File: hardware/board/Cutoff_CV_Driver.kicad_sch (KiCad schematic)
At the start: 17 parts

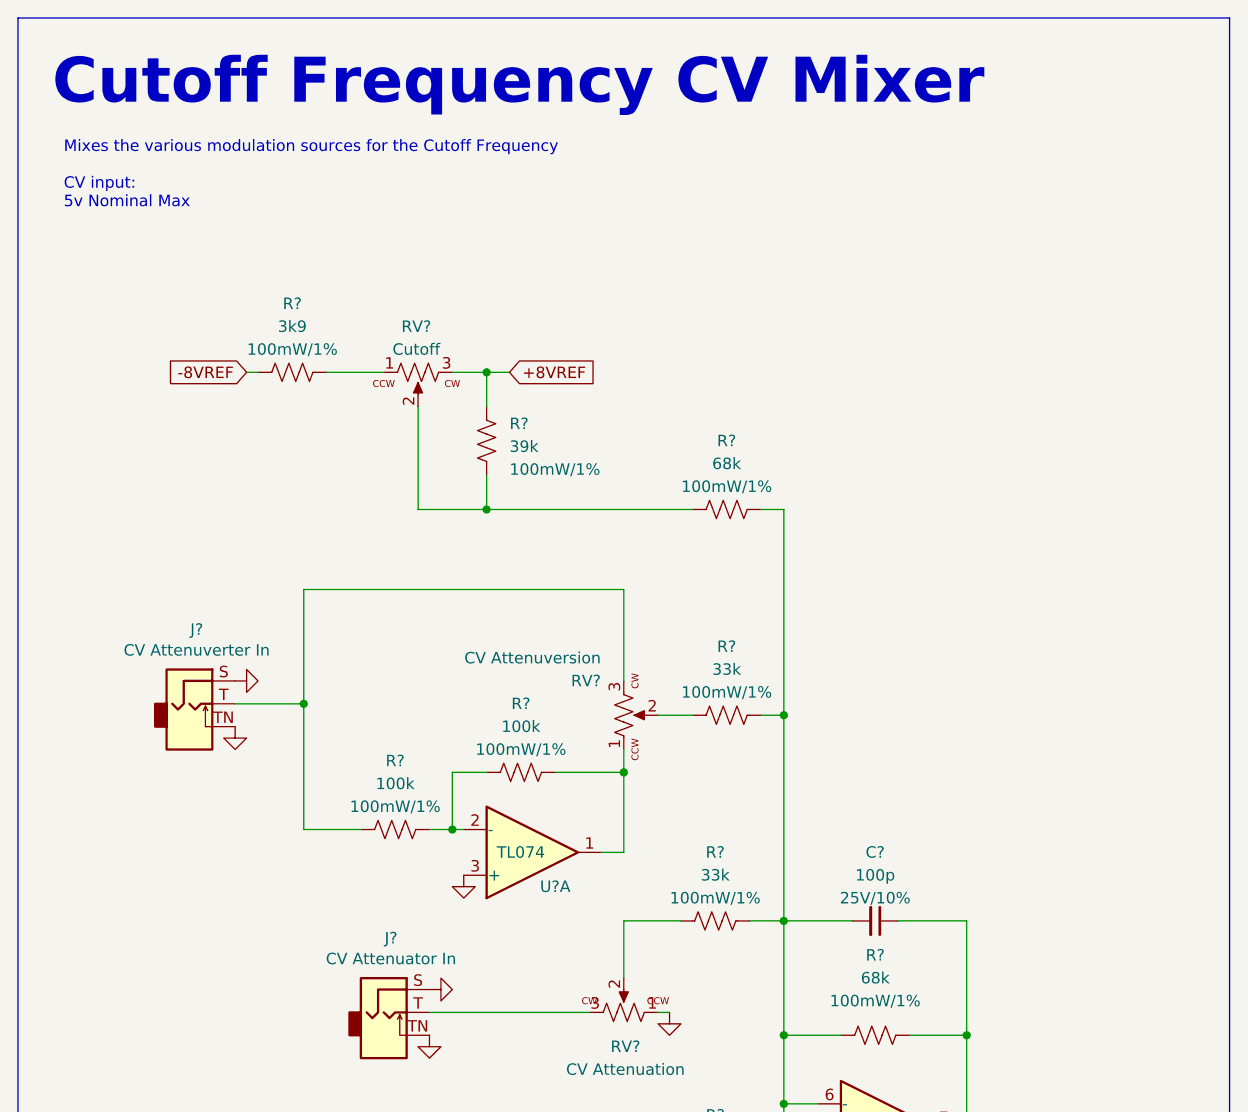
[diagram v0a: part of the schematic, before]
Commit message: Schematic getting closer to being finished
Schematic should be close to being ready to assign MPNs.
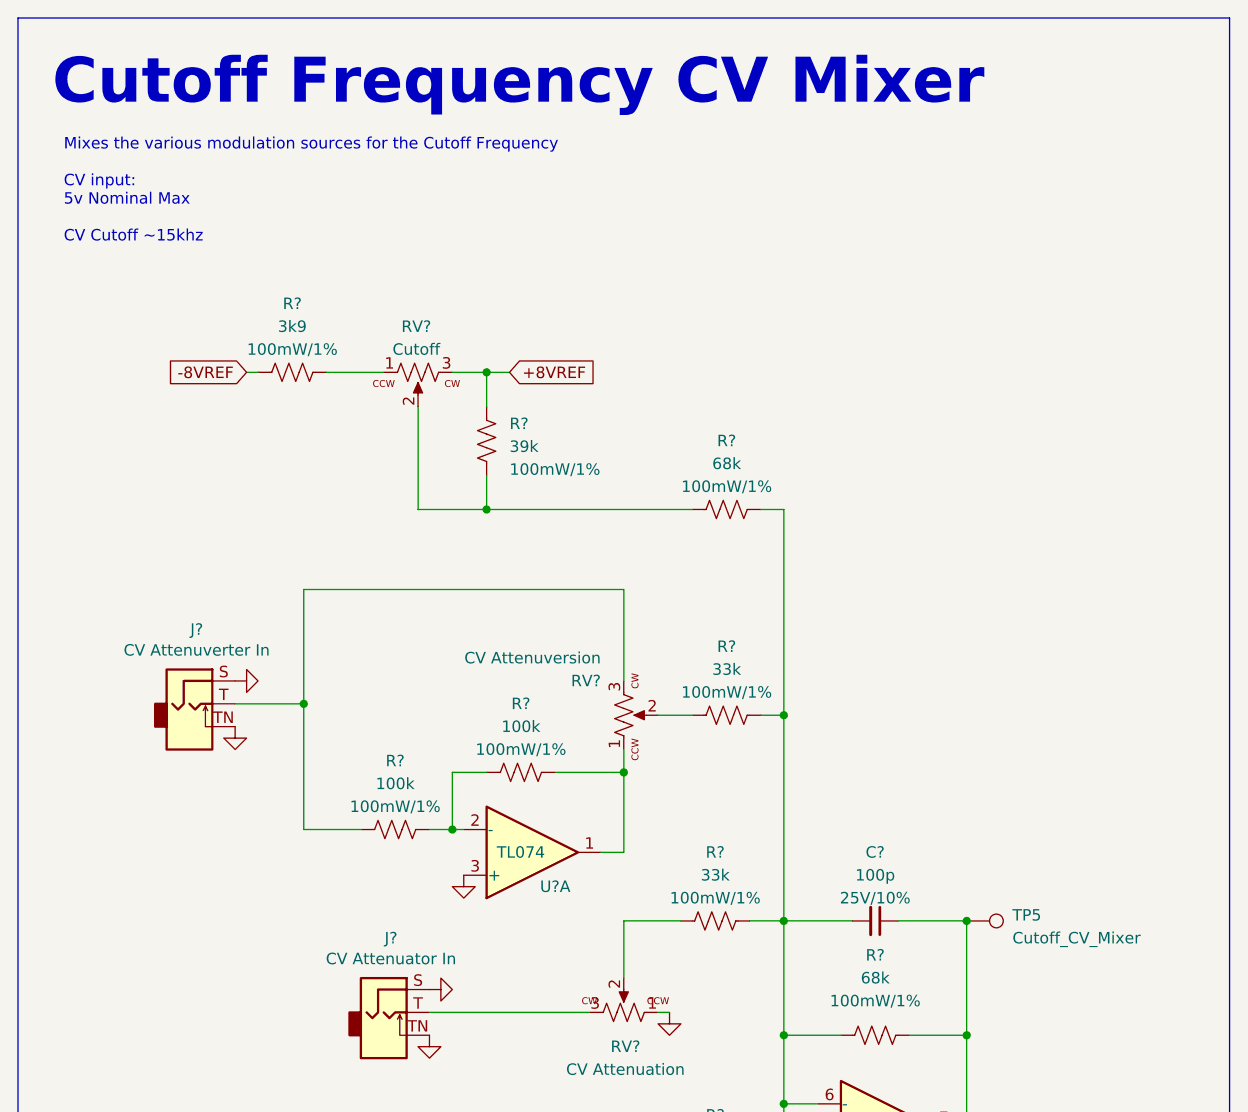
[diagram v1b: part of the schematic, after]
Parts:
- added TP5: Cutoff_CV_Mixer, symbol Connector:TestPoint
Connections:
- net CUTOFF_OUT: now also TP5.1
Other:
- note added: "Mixes the various modulation sources for the Cutoff Frequency CV input: 5v Nominal Max CV Cutoff ~15khz"
- note removed: "Mixes the various modulation sources for the Cutoff Frequency CV input: 5v Nominal Max"
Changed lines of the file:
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@@
   (junction (at 160.02 133.35) (diameter 0) (color 0 0 0 0)
   )
+  (junction (at 180.34 120.65) (diameter 0) (color 0 0 0 0)
+  )
   (junction (at 160.02 97.79) (diameter 0) (color 0 0 0 0)
   )
@@
     (stroke (width 0) (type default))
   )
+  (wire (pts (xy 180.34 120.65) (xy 180.34 133.35))
+    (stroke (width 0) (type default))
+  )
   (wire (pts (xy 127 59.69) (xy 127 63.5))
     (stroke (width 0) (type default))
@@
     (stroke (width 0) (type default))
   )
-  (wire (pts (xy 180.34 120.65) (xy 180.34 133.35))
-    (stroke (width 0) (type default))
-  )
   (wire (pts (xy 172.72 120.65) (xy 180.34 120.65))
     (stroke (width 0) (type default))
@@
     (fill (type none))
   )
-  (text "Mixes the various modulation sources for the Cutoff Frequency\n\nCV input:\n5v Nominal Max\n\n\n"
-    (at 80.01 45.72 0)
+  (text "Mixes the various modulation sources for the Cutoff Frequency\n\nCV input:\n5v Nominal Max\n\nCV Cutoff ~15khz\n\n\n"
+    (at 80.01 49.53 0)
     (effects (font (size 1.27 1.27)) (justify left bottom))
   )
@@
         )
       )
+    )
+  )
+  (symbol (lib_id "Connector:TestPoint") (at 180.34 120.65 270) (unit 1)
+    (in_bom yes) (on_board yes) (dnp no) (fields_autoplaced)
+    (property "Reference" "TP5" (at 185.42 120.015 90)
+      (effects (font (size 1.27 1.27)) (justify left))
+    )
+    (property "Value" "Cutoff_CV_Mixer" (at 185.42 122.555 90)
+      (effects (font (size 1.27 1.27)) (justify left))
+    )
+    (property "Footprint" "" (at 180.34 125.73 0)
+      (effects (font (size 1.27 1.27)) hide)
+    )
+    (property "Datasheet" "~" (at 180.34 125.73 0)
+      (effects (font (size 1.27 1.27)) hide)
+    )
+    (pin "1")
+    (instances
+      (project "mainboard"
+        (path "/960bd036-bf0c-45ea-9f41-1321756e0e5a/48d891c0-35ba-4c8e-a930-c990a10298eb"
+          (reference "TP5") (unit 1)
+        )
+        (path "/960bd036-bf0c-45ea-9f41-1321756e0e5a/193c5b93-4c44-4f6f-9ef0-5f8993e4582d"
+          (reference "TP13") (unit 1)
+        )
+      )
